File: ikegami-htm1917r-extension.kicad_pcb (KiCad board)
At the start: 2 copper layers, 190 x 200 mm, 2 parts, among them J10 DIN41612_02x32_AB, J20 DIN41612_02x32_AB

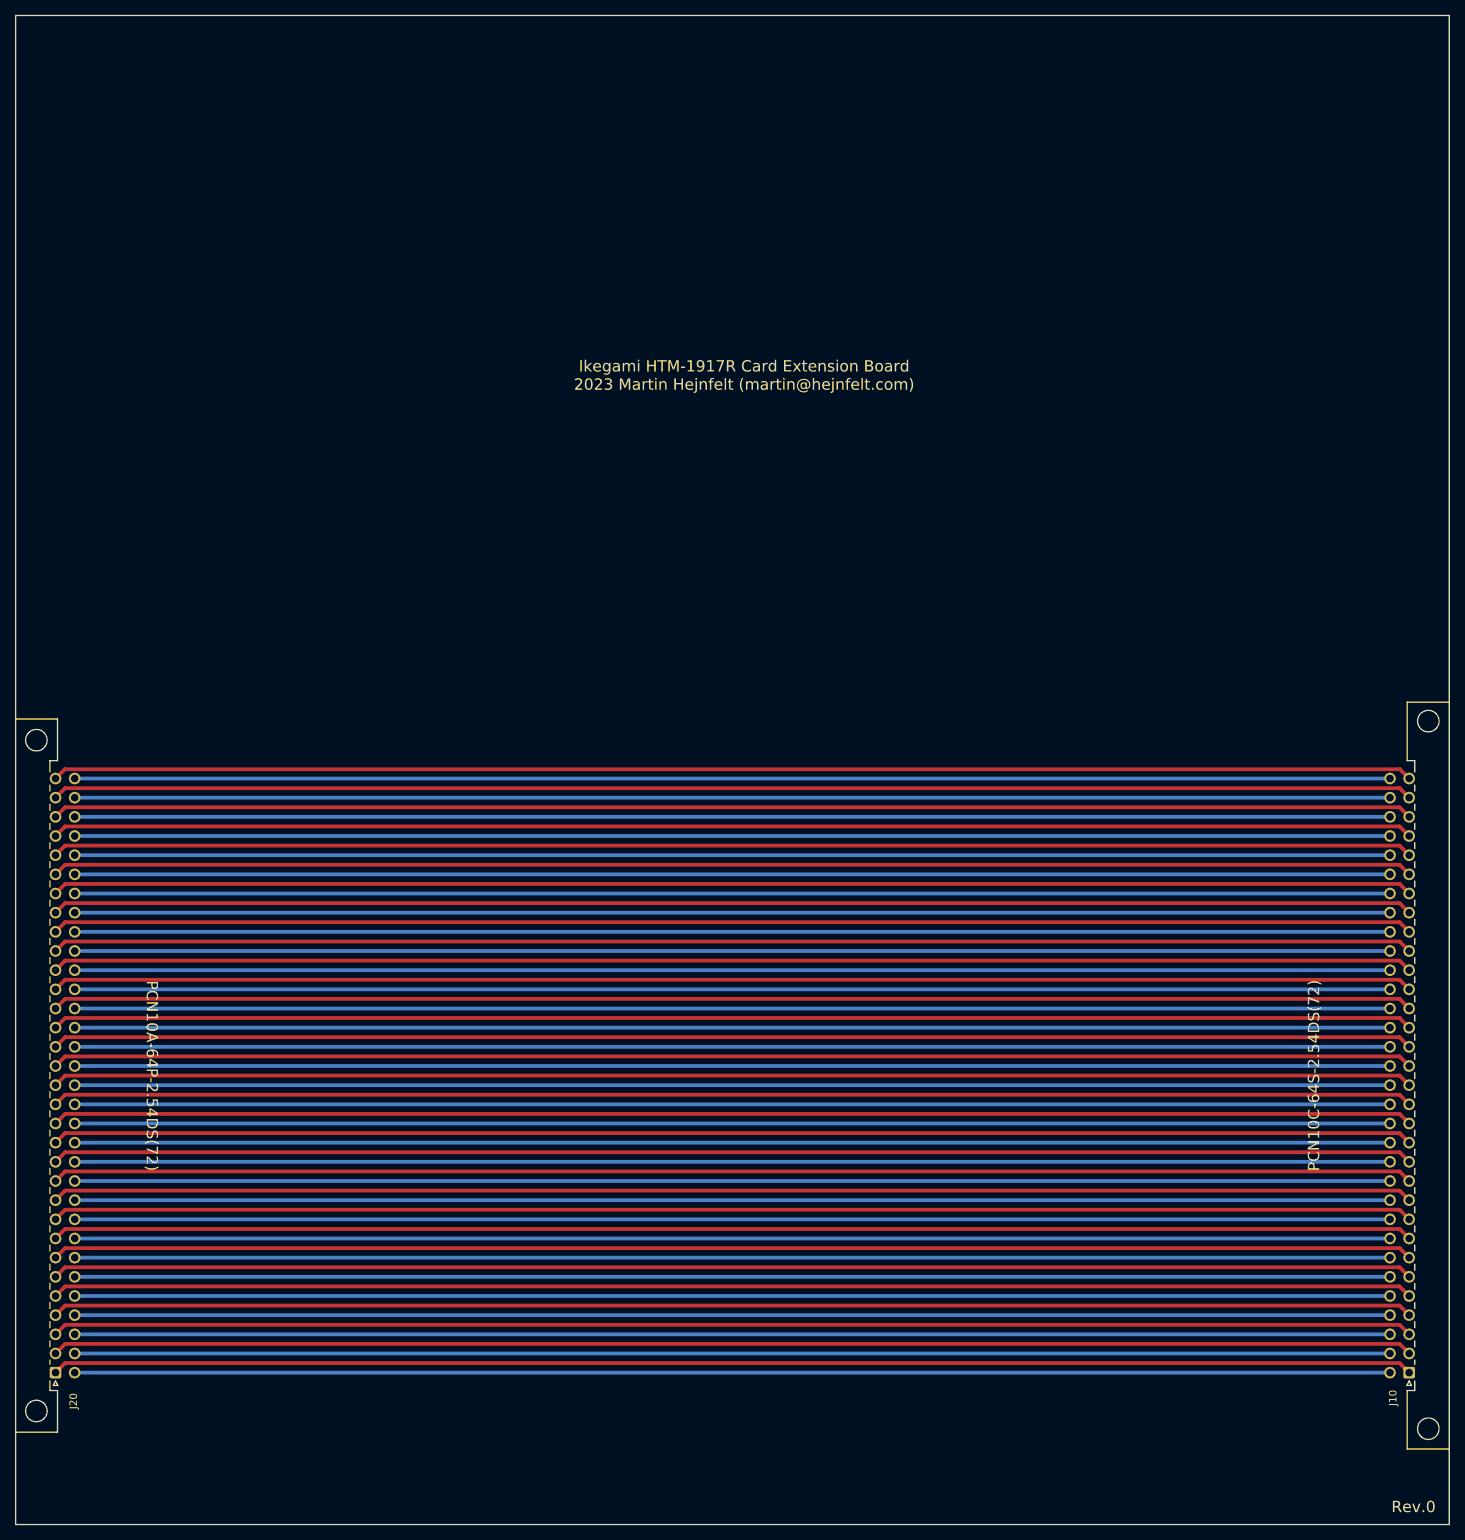
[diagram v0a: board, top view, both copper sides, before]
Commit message: Moved connectors a bit, added missing footprint
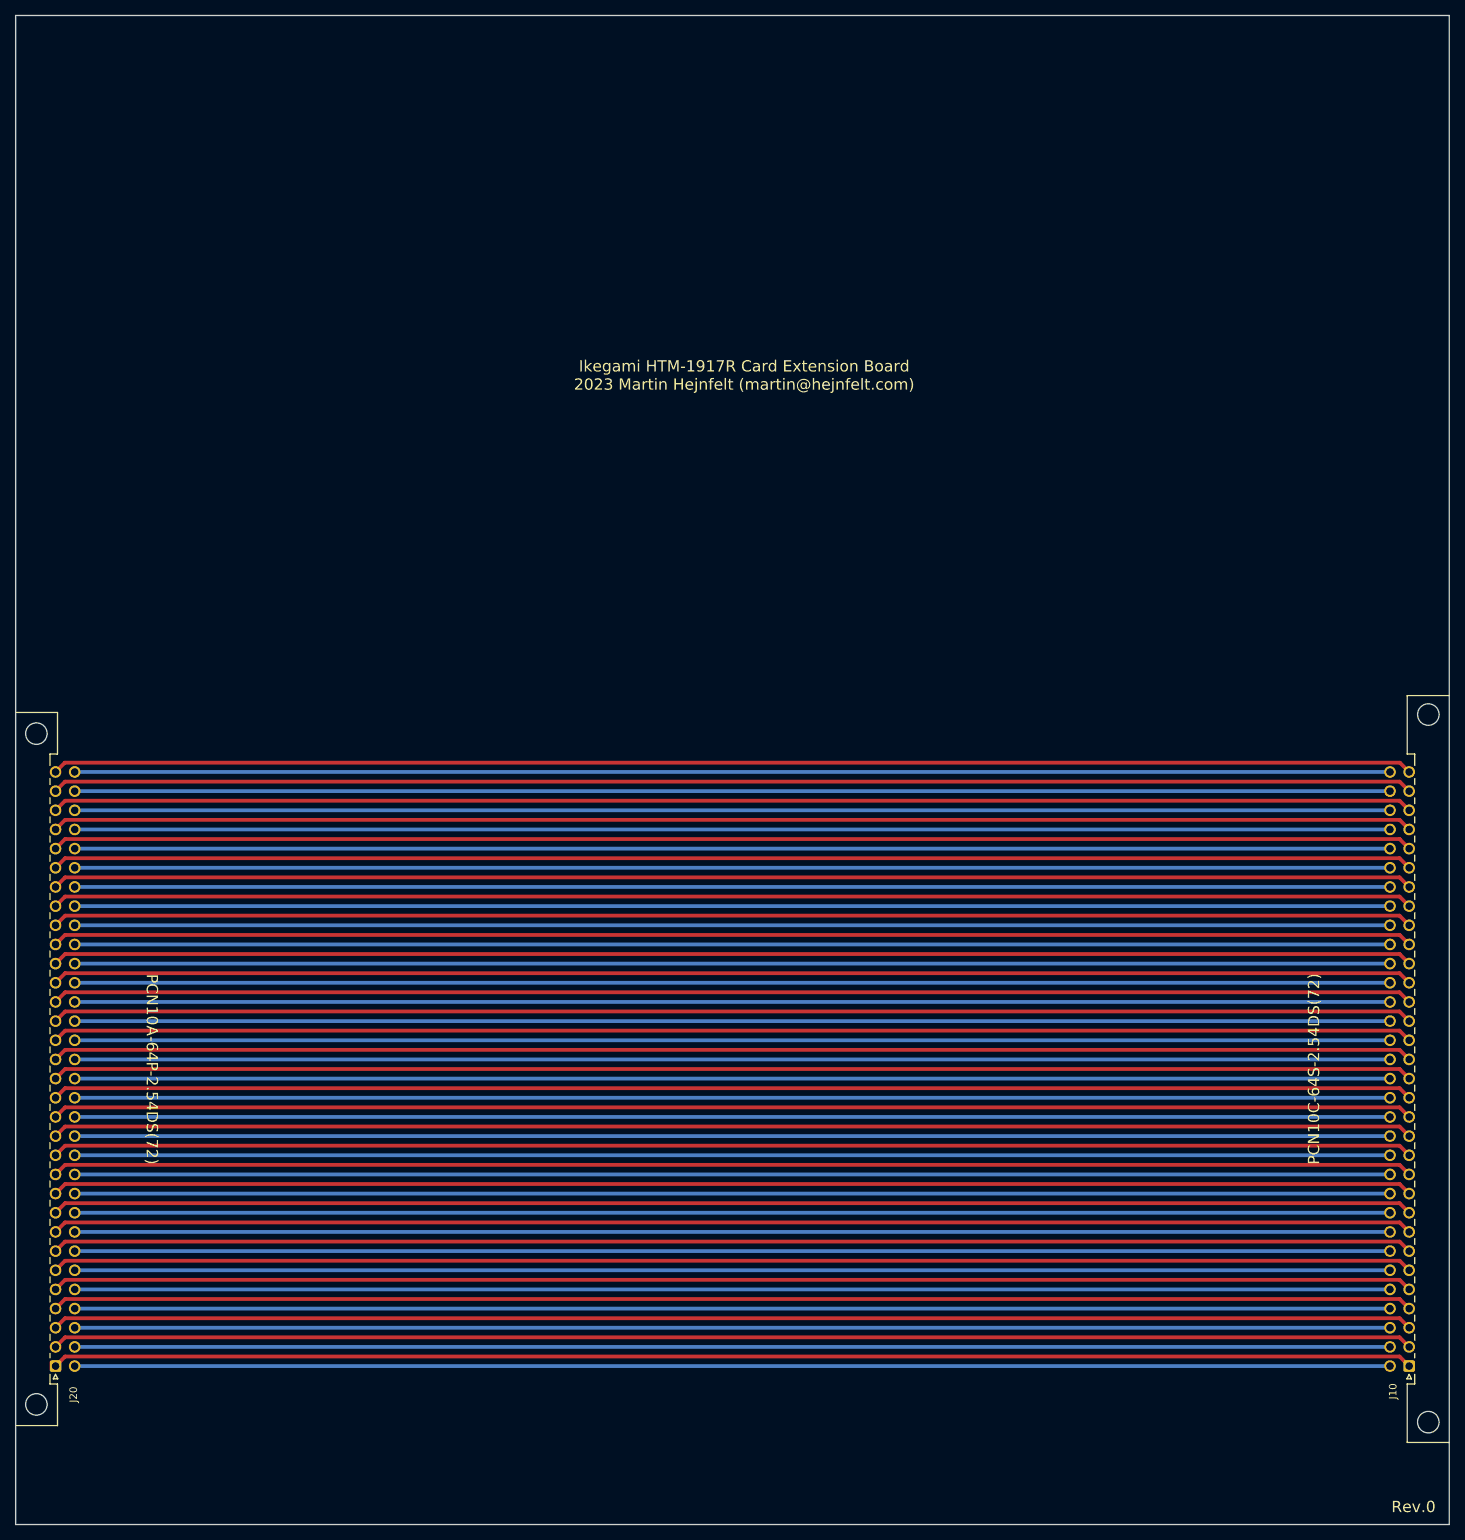
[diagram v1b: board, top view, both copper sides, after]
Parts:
- moved J10 0.87 mm to (257.7, 232.0)
- moved J20 0.87 mm to (78.3, 232.0)
